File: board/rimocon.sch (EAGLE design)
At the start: 10 parts

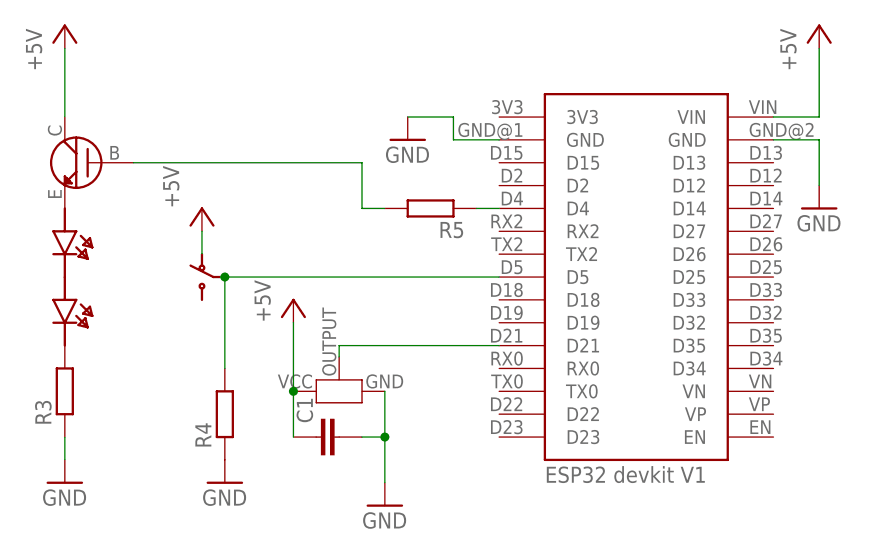
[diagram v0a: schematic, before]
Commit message: 送受信表示の統合とそれに伴う回路修正
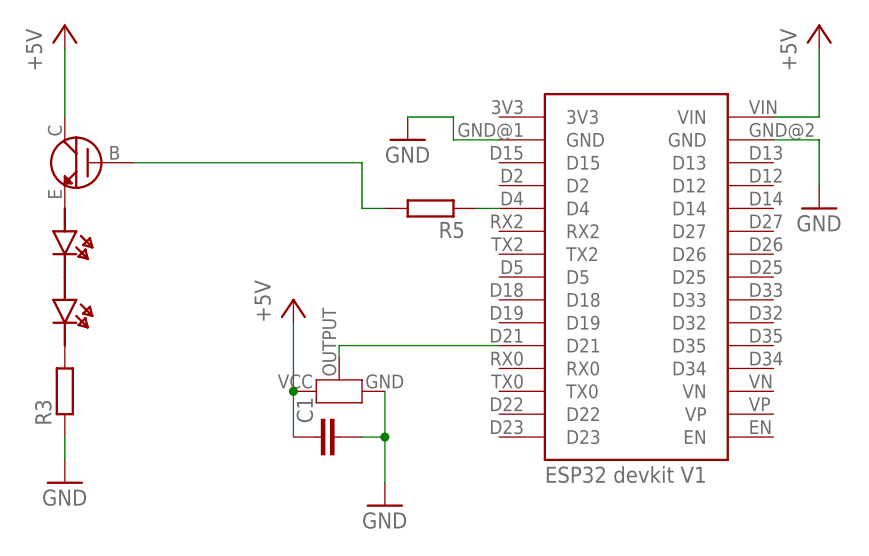
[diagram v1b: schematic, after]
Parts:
- removed R4: (no value), my_rcl:R-EU_0204/5
- removed U$4: SWITCHSWTICH_SLIDE, Custom_Parts:SWITCHSWTICH_SLIDE
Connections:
- removed net N$7: R4.2, U$3.D5, U$4.IN
- net +5V: no longer U$4.OUT1
- net GND: no longer R4.1
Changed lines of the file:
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@@
 <part name="P+3" library="supply1" library_urn="urn:adsk.eagle:library:371" deviceset="+5V" device=""/>
 <part name="GND1" library="supply1" library_urn="urn:adsk.eagle:library:371" deviceset="GND" device=""/>
-<part name="U$4" library="Custom_Parts" deviceset="SWITCH" device="SWTICH_SLIDE"/>
-<part name="P+4" library="supply1" library_urn="urn:adsk.eagle:library:371" deviceset="+5V" device=""/>
-<part name="GND5" library="supply1" library_urn="urn:adsk.eagle:library:371" deviceset="GND" device=""/>
 <part name="R3" library="my_rcl" deviceset="R-EU_" device="0204/5"/>
-<part name="R4" library="my_rcl" deviceset="R-EU_" device="0204/5"/>
 <part name="R5" library="my_rcl" deviceset="R-EU_" device="0204/5"/>
 <part name="U$5" library="Custom_Parts" deviceset="LED" device="OSI5FU3A11C"/>
@@
 <attribute name="VALUE" x="-10.16" y="10.16" size="1.778" layer="96"/>
 </instance>
-<instance part="U$4" gate="G$1" x="-27.94" y="38.1" smashed="yes"/>
-<instance part="P+4" gate="1" x="-27.94" y="45.72" smashed="yes">
-<attribute name="VALUE" x="-30.48" y="45.72" size="1.778" layer="96" rot="R90"/>
-</instance>
-<instance part="GND5" gate="1" x="-25.4" y="15.24" smashed="yes">
-<attribute name="VALUE" x="-27.94" y="12.7" size="1.778" layer="96"/>
-</instance>
 <instance part="R3" gate="G$1" x="-43.18" y="25.4" smashed="yes" rot="R90">
 <attribute name="NAME" x="-44.6786" y="21.59" size="1.778" layer="95" rot="R90"/>
 <attribute name="VALUE" x="-39.878" y="21.59" size="1.778" layer="96" rot="R90"/>
-</instance>
-<instance part="R4" gate="G$1" x="-25.4" y="22.86" smashed="yes" rot="R90">
-<attribute name="NAME" x="-26.8986" y="19.05" size="1.778" layer="95" rot="R90"/>
-<attribute name="VALUE" x="-22.098" y="19.05" size="1.778" layer="96" rot="R90"/>
 </instance>
 <instance part="R5" gate="G$1" x="-2.54" y="45.72" smashed="yes" rot="R180">
@@
 <pinref part="R3" gate="G$1" pin="1"/>
 </segment>
-<segment>
-<pinref part="GND5" gate="1" pin="GND"/>
-<pinref part="R4" gate="G$1" pin="1"/>
-</segment>
 </net>
 <net name="N$3" class="0">
@@
 </segment>
 <segment>
-<pinref part="U$4" gate="G$1" pin="OUT1"/>
-<pinref part="P+4" gate="1" pin="+5V"/>
-<wire x1="-27.94" y1="40.64" x2="-27.94" y2="43.18" width="0.1524" layer="91"/>
-</segment>
-<segment>
 <pinref part="P+3" gate="1" pin="+5V"/>
 <pinref part="U$2" gate="G$1" pin="VCC"/>
@@
 </segment>
 </net>
-<net name="N$7" class="0">
-<segment>
-<pinref part="U$4" gate="G$1" pin="IN"/>
-<junction x="-25.4" y="38.1"/>
-<pinref part="U$3" gate="G$1" pin="D5"/>
-<wire x1="5.08" y1="38.1" x2="-25.4" y2="38.1" width="0.1524" layer="91"/>
-<wire x1="-25.4" y1="38.1" x2="-25.4" y2="27.94" width="0.1524" layer="91"/>
-<pinref part="R4" gate="G$1" pin="2"/>
-</segment>
-</net>

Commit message: 回路をエミッタ設置へと変更 単ボタンリモコン用繰り返し処理の実装
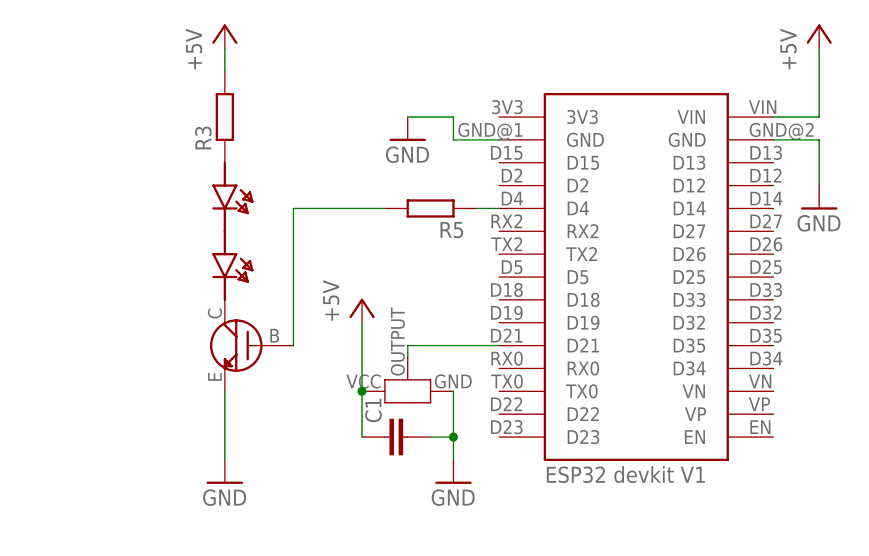
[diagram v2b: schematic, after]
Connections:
- net +5V: now also R3.2; no longer U$1.C
- net GND: now also U$1.E; no longer R3.1
- net N$1: now also U$1.C, U$5.CATHODE; no longer U$1.E, U$6.ANODE
- net N$2: now also R3.1, U$6.ANODE; no longer R3.2, U$5.CATHODE
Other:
- moved on the sheet: C1, R3
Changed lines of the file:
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@@
 </plain>
 <instances>
-<instance part="U$1" gate="G$1" x="-40.64" y="50.8" smashed="yes" rot="MR0"/>
-<instance part="GND2" gate="1" x="-43.18" y="15.24" smashed="yes">
-<attribute name="VALUE" x="-45.72" y="12.7" size="1.778" layer="96"/>
+<instance part="U$1" gate="G$1" x="-22.86" y="30.48" smashed="yes" rot="MR0"/>
+<instance part="GND2" gate="1" x="-25.4" y="15.24" smashed="yes">
+<attribute name="VALUE" x="-27.94" y="12.7" size="1.778" layer="96"/>
 </instance>
 <instance part="U$3" gate="G$1" x="20.32" y="38.1" smashed="yes"/>
@@
 <attribute name="VALUE" x="38.1" y="43.18" size="1.778" layer="96"/>
 </instance>
-<instance part="P+2" gate="1" x="-43.18" y="66.04" smashed="yes">
-<attribute name="VALUE" x="-45.72" y="60.96" size="1.778" layer="96" rot="R90"/>
+<instance part="P+2" gate="1" x="-25.4" y="66.04" smashed="yes">
+<attribute name="VALUE" x="-27.94" y="60.96" size="1.778" layer="96" rot="R90"/>
 </instance>
-<instance part="U$2" gate="G$1" x="-12.7" y="25.4" smashed="yes" rot="MR270"/>
-<instance part="P+3" gate="1" x="-17.78" y="35.56" smashed="yes">
-<attribute name="VALUE" x="-20.32" y="33.02" size="1.778" layer="96" rot="R90"/>
+<instance part="U$2" gate="G$1" x="-5.08" y="25.4" smashed="yes" rot="MR270"/>
+<instance part="P+3" gate="1" x="-10.16" y="35.56" smashed="yes">
+<attribute name="VALUE" x="-12.7" y="33.02" size="1.778" layer="96" rot="R90"/>
 </instance>
-<instance part="GND1" gate="1" x="-7.62" y="12.7" smashed="yes">
-<attribute name="VALUE" x="-10.16" y="10.16" size="1.778" layer="96"/>
+<instance part="GND1" gate="1" x="0" y="15.24" smashed="yes">
+<attribute name="VALUE" x="-2.54" y="12.7" size="1.778" layer="96"/>
 </instance>
-<instance part="R3" gate="G$1" x="-43.18" y="25.4" smashed="yes" rot="R90">
-<attribute name="NAME" x="-44.6786" y="21.59" size="1.778" layer="95" rot="R90"/>
-<attribute name="VALUE" x="-39.878" y="21.59" size="1.778" layer="96" rot="R90"/>
+<instance part="R3" gate="G$1" x="-25.4" y="55.88" smashed="yes" rot="R90">
+<attribute name="NAME" x="-26.8986" y="52.07" size="1.778" layer="95" rot="R90"/>
+<attribute name="VALUE" x="-22.098" y="52.07" size="1.778" layer="96" rot="R90"/>
 </instance>
 <instance part="R5" gate="G$1" x="-2.54" y="45.72" smashed="yes" rot="R180">
@@
 <attribute name="VALUE" x="1.27" y="49.022" size="1.778" layer="96" rot="R180"/>
 </instance>
-<instance part="U$5" gate="G$1" x="-43.18" y="33.02" smashed="yes" rot="R270"/>
-<instance part="U$6" gate="G$1" x="-43.18" y="40.64" smashed="yes" rot="R270"/>
-<instance part="C1" gate="G$1" x="-15.24" y="20.32" smashed="yes" rot="R90">
-<attribute name="NAME" x="-15.621" y="21.844" size="1.778" layer="95" rot="R90"/>
-<attribute name="VALUE" x="-10.541" y="21.844" size="1.778" layer="96" rot="R90"/>
+<instance part="U$5" gate="G$1" x="-25.4" y="38.1" smashed="yes" rot="R270"/>
+<instance part="U$6" gate="G$1" x="-25.4" y="45.72" smashed="yes" rot="R270"/>
+<instance part="C1" gate="G$1" x="-7.62" y="20.32" smashed="yes" rot="R90">
+<attribute name="NAME" x="-8.001" y="21.844" size="1.778" layer="95" rot="R90"/>
+<attribute name="VALUE" x="-2.921" y="21.844" size="1.778" layer="96" rot="R90"/>
 </instance>
 </instances>
@@
 <pinref part="GND1" gate="1" pin="GND"/>
 <pinref part="U$2" gate="G$1" pin="GND"/>
-<wire x1="-7.62" y1="15.24" x2="-7.62" y2="20.32" width="0.1524" layer="91"/>
+<wire x1="0" y1="17.78" x2="0" y2="20.32" width="0.1524" layer="91"/>
 <pinref part="C1" gate="G$1" pin="2"/>
-<wire x1="-7.62" y1="20.32" x2="-7.62" y2="25.4" width="0.1524" layer="91"/>
-<wire x1="-10.16" y1="20.32" x2="-7.62" y2="20.32" width="0.1524" layer="91"/>
-<junction x="-7.62" y="20.32"/>
+<wire x1="0" y1="20.32" x2="0" y2="25.4" width="0.1524" layer="91"/>
+<wire x1="-2.54" y1="20.32" x2="0" y2="20.32" width="0.1524" layer="91"/>
+<junction x="0" y="20.32"/>
 </segment>
 <segment>
+<pinref part="U$1" gate="G$1" pin="E"/>
 <pinref part="GND2" gate="1" pin="GND"/>
-<wire x1="-43.18" y1="17.78" x2="-43.18" y2="20.32" width="0.1524" layer="91"/>
-<pinref part="R3" gate="G$1" pin="1"/>
+<wire x1="-25.4" y1="25.4" x2="-25.4" y2="17.78" width="0.1524" layer="91"/>
 </segment>
 </net>
@@
 </segment>
 <segment>
-<pinref part="P+2" gate="1" pin="+5V"/>
-<pinref part="U$1" gate="G$1" pin="C"/>
-<wire x1="-43.18" y1="63.5" x2="-43.18" y2="55.88" width="0.1524" layer="91"/>
+<pinref part="P+3" gate="1" pin="+5V"/>
+<pinref part="U$2" gate="G$1" pin="VCC"/>
+<wire x1="-10.16" y1="33.02" x2="-10.16" y2="25.4" width="0.1524" layer="91"/>
+<pinref part="C1" gate="G$1" pin="1"/>
+<wire x1="-10.16" y1="25.4" x2="-10.16" y2="20.32" width="0.1524" layer="91"/>
+<junction x="-10.16" y="25.4"/>
 </segment>
 <segment>
-<pinref part="P+3" gate="1" pin="+5V"/>
-<pinref part="U$2" gate="G$1" pin="VCC"/>
-<wire x1="-17.78" y1="33.02" x2="-17.78" y2="25.4" width="0.1524" layer="91"/>
-<pinref part="C1" gate="G$1" pin="1"/>
-<wire x1="-17.78" y1="25.4" x2="-17.78" y2="20.32" width="0.1524" layer="91"/>
-<junction x="-17.78" y="25.4"/>
+<pinref part="P+2" gate="1" pin="+5V"/>
+<pinref part="R3" gate="G$1" pin="2"/>
+<wire x1="-25.4" y1="60.96" x2="-25.4" y2="63.5" width="0.1524" layer="91"/>
 </segment>
 </net>
@@
 <segment>
 <pinref part="U$1" gate="G$1" pin="B"/>
-<wire x1="-35.56" y1="50.8" x2="-10.16" y2="50.8" width="0.1524" layer="91"/>
-<wire x1="-10.16" y1="50.8" x2="-10.16" y2="45.72" width="0.1524" layer="91"/>
-<wire x1="-10.16" y1="45.72" x2="-7.62" y2="45.72" width="0.1524" layer="91"/>
+<wire x1="-17.78" y1="30.48" x2="-17.78" y2="45.72" width="0.1524" layer="91"/>
+<wire x1="-17.78" y1="45.72" x2="-7.62" y2="45.72" width="0.1524" layer="91"/>
 <pinref part="R5" gate="G$1" pin="2"/>
 </segment>
@@
 <segment>
 <pinref part="U$2" gate="G$1" pin="OUTPUT"/>
-<wire x1="-12.7" y1="30.48" x2="-12.7" y2="29.21" width="0.1524" layer="91"/>
+<wire x1="-5.08" y1="30.48" x2="-5.08" y2="29.21" width="0.1524" layer="91"/>
 <pinref part="U$3" gate="G$1" pin="D21"/>
-<wire x1="-12.7" y1="30.48" x2="5.08" y2="30.48" width="0.1524" layer="91"/>
+<wire x1="-5.08" y1="30.48" x2="5.08" y2="30.48" width="0.1524" layer="91"/>
 </segment>
 </net>
@@
 <net name="N$1" class="0">
 <segment>
-<pinref part="U$1" gate="G$1" pin="E"/>
-<pinref part="U$6" gate="G$1" pin="ANODE"/>
+<pinref part="U$1" gate="G$1" pin="C"/>
+<pinref part="U$5" gate="G$1" pin="CATHODE"/>
 </segment>
 </net>
 <net name="N$2" class="0">
 <segment>
-<pinref part="U$5" gate="G$1" pin="CATHODE"/>
-<pinref part="R3" gate="G$1" pin="2"/>
+<pinref part="U$6" gate="G$1" pin="ANODE"/>
+<pinref part="R3" gate="G$1" pin="1"/>
 </segment>
 </net>
